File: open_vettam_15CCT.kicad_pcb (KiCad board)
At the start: 2 copper layers, 68.2 x 49 mm, 60 parts, among them IC1 ESP32-C6-MINI-1-N4, IC2 TPS922053DRRR, IC3 TPS922053DRRR, IC4 LMR51610YDBVR, J1 24VIN, J2 DEBUG, J3 LED_OUT, J5 TEMP_IN, Q1 SQJ457EP-T1_BE3

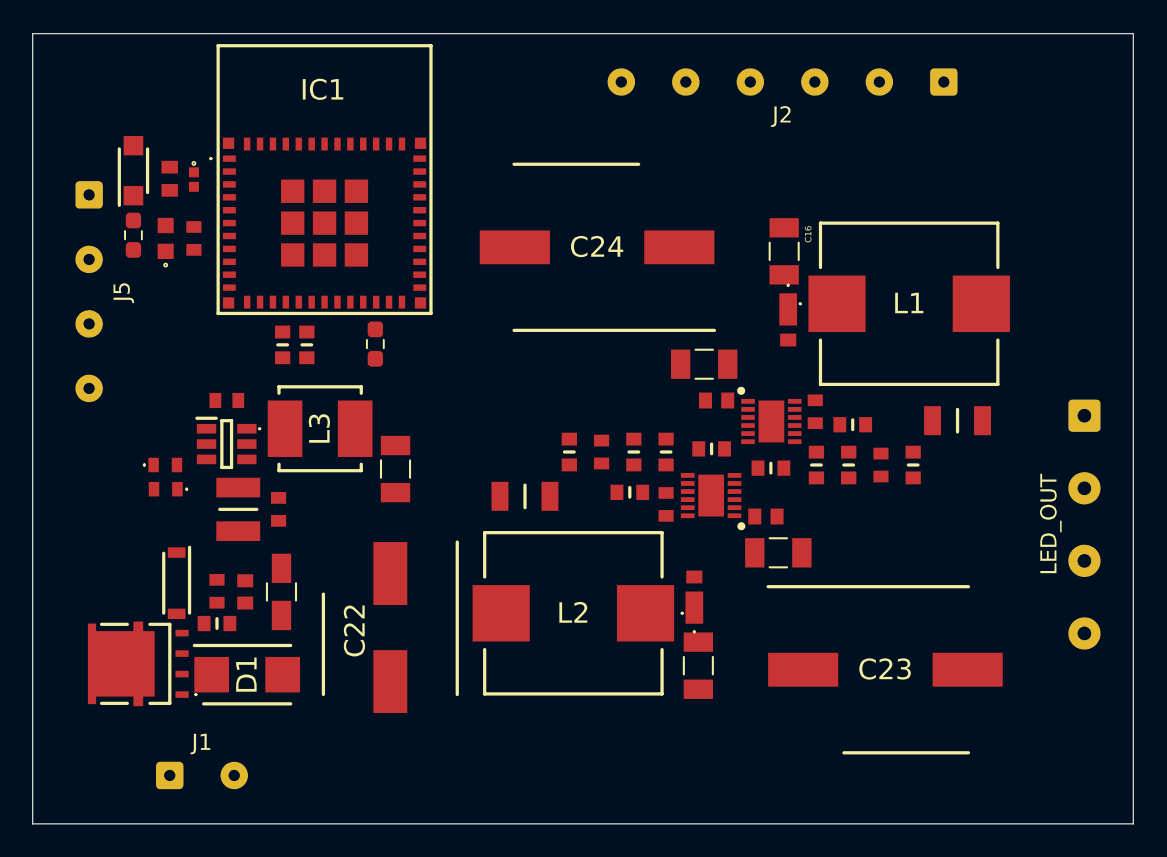
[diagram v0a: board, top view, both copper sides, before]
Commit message: Finalize KiCad PCB sources for 5-piece test build
Commit the completed Open Vettam 15CCT KiCad source design files prepared for the initial five-piece production test run.

Included files are limited to the schematic hierarchy, PCB layouts, KiCad project files, and the LED MCPCB design-rules file. Generated BOM exports, fabrication output archives, freerouting/temp files, logs, backups, images, netlists, and Altium import artifacts are intentionally left unstaged.

Updated main controller board sources:

- open_vettam_15CCT.kicad_sch

- open_vettam_15CCT.kicad_pcb

- open_vettam_15CCT.kicad_pro

- 24v_Input.kicad_sch

- 24-5_buck.kicad_sch

- MCU.kicad_sch

- cc_driver.kicad_sch

Updated LED MCPCB sources:

- led_mcpcb/led_mcpcb.kicad_sch

- led_mcpcb/led_mcpcb.kicad_pcb

- led_mcpcb/led_mcpcb.kicad_pro

- led_mcpcb/led_mcpcb.kicad_dru

- led_mcpcb/CW-5000.kicad_sch

- led_mcpcb/WW-3000.kicad_sch

- led_mcpcb/digital_temp.kicad_sch
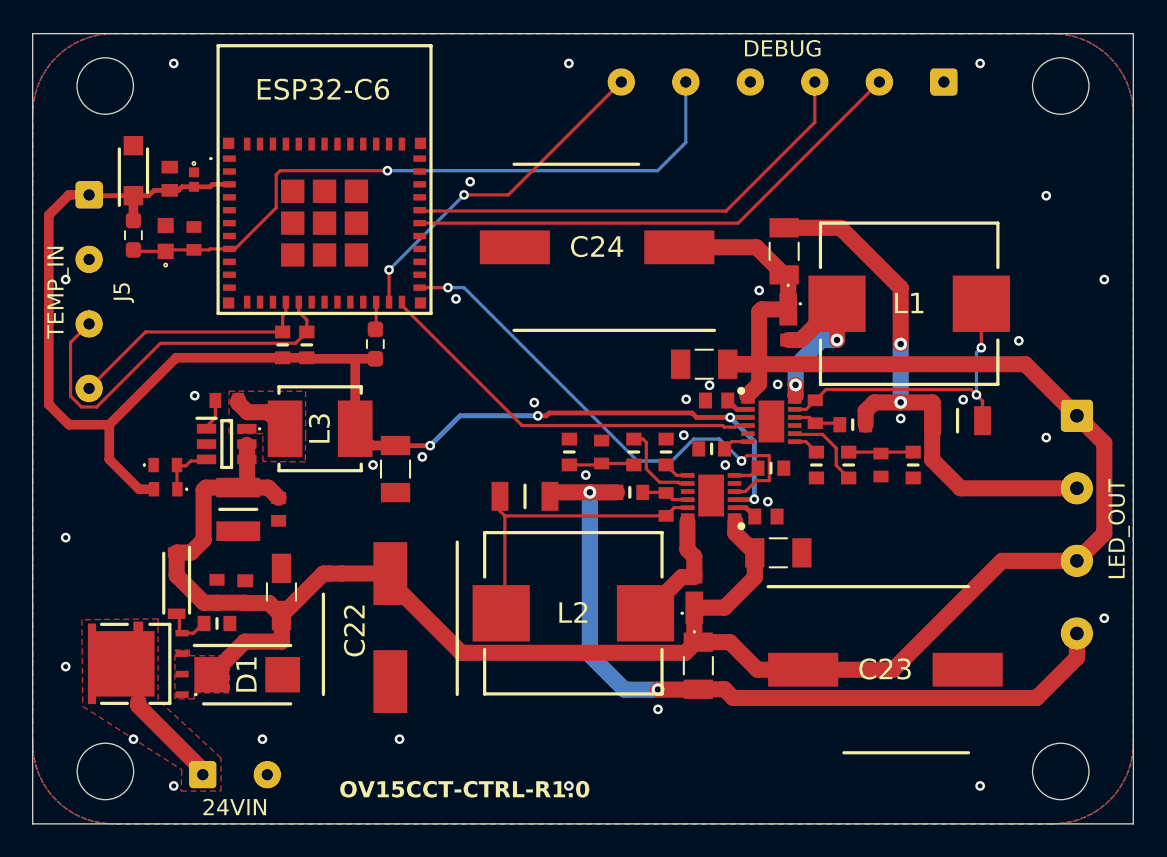
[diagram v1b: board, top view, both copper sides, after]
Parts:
- moved J1 2.05 mm to (128.3, 100.7)
- moved J3 0.47 mm to (182.5, 78.4)
- renumbered IC1 to ESP32-C6
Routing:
- net +24V: track 0.00 -> 148.2 mm
- net +3V3: track 0.00 -> 90.6 mm, vias 0 -> 4
- net /CC_Driver/CW-: track 0.00 -> 48.2 mm, vias 0 -> 2
- net /MCU/RST: track 0.00 -> 42.0 mm, vias 0 -> 1
- net /CC_Driver/WW-: track 0.00 -> 34.4 mm, vias 0 -> 2
- net /MCU/RX: track 0.00 -> 32.1 mm
- net /CC_Driver/PWM_CW: track 0.00 -> 31.4 mm, vias 0 -> 2
- net /MCU/TX: track 0.00 -> 29.3 mm
- net /CC_Driver/PWM_WW: track 0.00 -> 24.8 mm
- net /MCU/SCL: track 0.00 -> 23.9 mm
- net /MCU/<NO NET>: track 0.00 -> 21.2 mm, vias 0 -> 2
- net Net-(IC2-CSN): track 0.00 -> 19.4 mm, vias 0 -> 2
- net Net-(IC3-CSN): track 0.00 -> 19.0 mm
- net /MCU/SDA: track 0.00 -> 15.4 mm
- net Net-(D3-A): track 0.00 -> 11.3 mm, vias 0 -> 2
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- added copper zone on F.Cu, net +24V
- added copper zone on B.Cu, net GND
- added copper zone on F.Cu, net GND
- added copper zone on F.Cu, net Net-(IC4-SW)
- added copper zone on F.Cu, net Net-(J1-Pin_1)
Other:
- outline, holes or cut-outs redrawn
- board text added: "OV15CCT-CTRL-R1.0"
